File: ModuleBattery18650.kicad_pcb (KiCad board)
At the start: 2 copper layers, 83 x 30 mm, 25 parts, among them J1 Connector_3p, J2 Connector_2p_r, T1 SISH101DN, T2 SISH101DN, T3 FDN337N, U1 MCP121T-315E

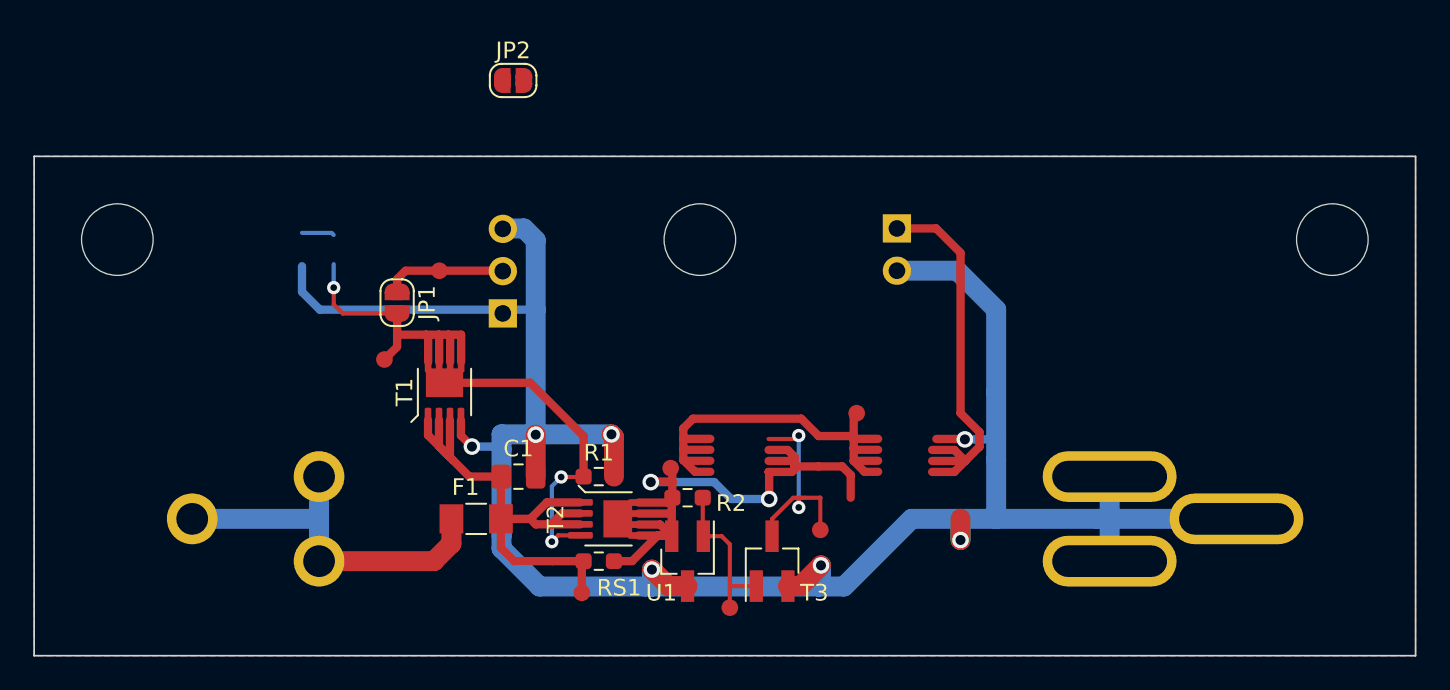
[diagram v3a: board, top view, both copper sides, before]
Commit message: Version 3
Fixed schematic. Combined charge subcircuit disable and low voltage circuit cutoff
charge connector now 3pin
removed charge input reverse polarity protection
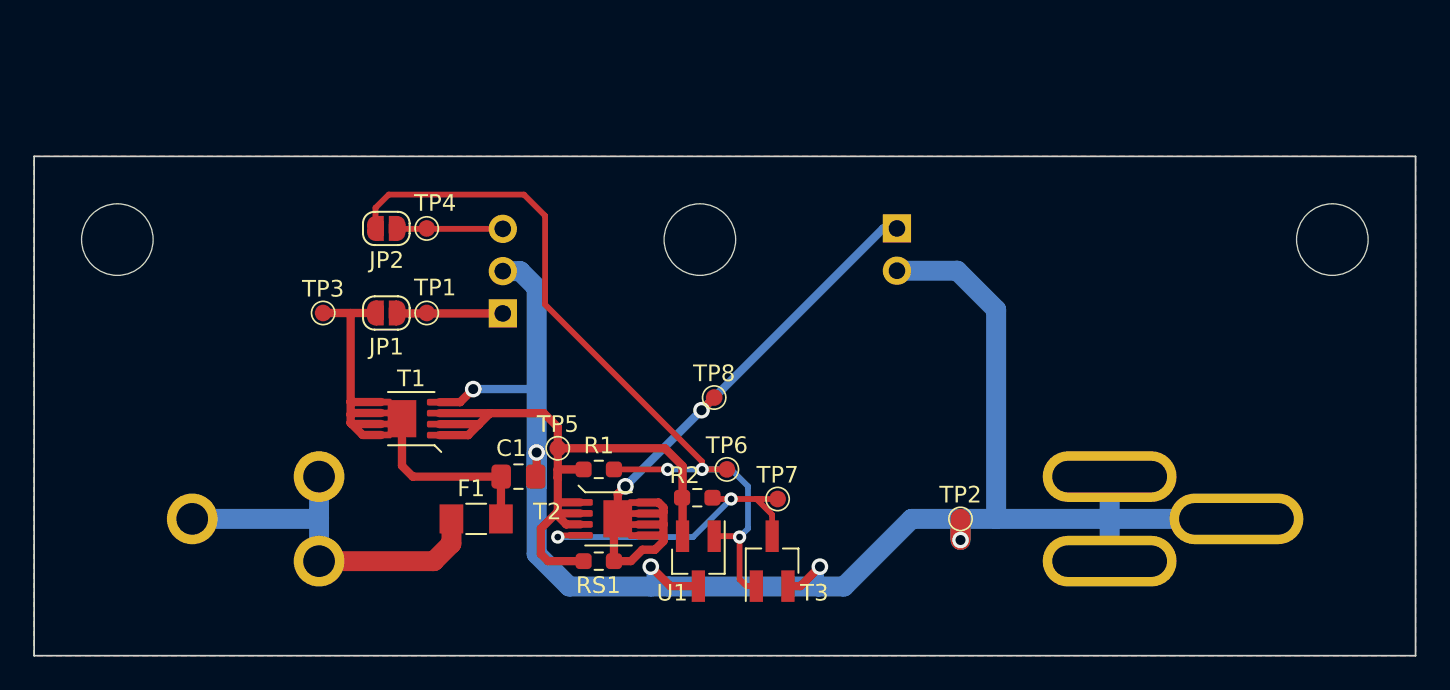
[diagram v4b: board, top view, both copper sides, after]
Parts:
- BT1: footprint 0ESN_Lib:18650_Battery_holder -> 0ESNLib:18650_Battery_holder
- F1: footprint 0ESN_Lib:Fuse_1206_3216Metric_Pad1.42x1.75mm_HandSolder -> 0ESNLib:Fuse_1206_3216Metric_Pad1.42x1.75mm_HandSolder
- J2: footprint 0ESN_Lib:Connector_2p_m -> 0ESNLib:Connector_2p_m
- T1, T2: footprint 0ESN_Lib:PowerPAK 1212-8S -> 0ESNLib:PowerPAK 1212-8S
- TP1, TP2, TP3, TP4, TP5, TP6, TP7, TP8: footprint 0ESN_Lib:TestPoint_Pad_D1.0mm -> 0ESNLib:TestPoint_Pad_D1.0mm
- moved TP4 23.8 mm to (132.6, 100.3)
- moved JP2 11.7 mm to (130.2, 100.3), turned to 180 degrees
- moved TP8 8.61 mm to (149.9, 110.5)
- moved TP6 8.31 mm to (150.6, 114.8)
- moved TP5 6.89 mm to (140.5, 113.5)
- moved TP3 4.62 mm to (126.4, 105.4)
- moved TP7 3.17 mm to (153.7, 116.6)
- moved TP1 2.65 mm to (132.6, 105.4)
- moved T1 2.56 mm to (131.7, 111.8), turned to 180 degrees
- moved JP1 0.90 mm to (130.2, 105.4), turned to 180 degrees
- moved U1 0.65 mm to (148.9, 120.3)
- moved R2 0.58 mm to (148.8, 116.5)
- moved R1 0.43 mm to (142.9, 114.8)
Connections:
- TP4 pad 1: Net-(JP2-B) -> Net-(J1-P3)
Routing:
- net (no net): track 121.9 -> 0.00 mm, vias 3 -> 0
- net Net-(JP2-B): track 0.00 -> 49.9 mm, vias 0 -> 3
- net Net-(U1-VDD): track 0.00 -> 43.0 mm, vias 2 -> 0
- net GND: track 136.5 -> 107.2 mm, vias 7 -> 5
- net Net-(JP1-B): track 0.00 -> 29.1 mm
- net /Vbat: track 53.1 -> 40.3 mm, vias 0 -> 2
- net Net-(J1-P3): track 0.00 -> 6.36 mm
- net Net-(T2-G): track 13.2 -> 19.3 mm
- net /Vch: track 7.32 -> 6.50 mm
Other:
- board text added: "ModuleBattery18650 Nicolas Esseiva V3_20230804"
- board text removed: "ModuleBattery18650 Nicolas Esseiva 2023.07.05 - r02"
